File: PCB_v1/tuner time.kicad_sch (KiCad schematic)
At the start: 1 part, among them J2 1051640001

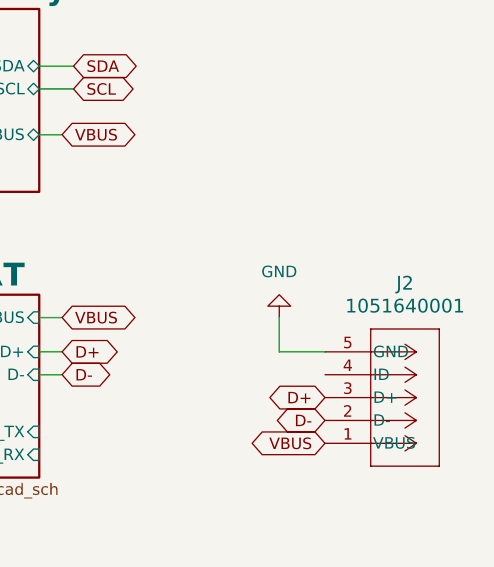
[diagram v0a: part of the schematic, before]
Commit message: adding the parts library
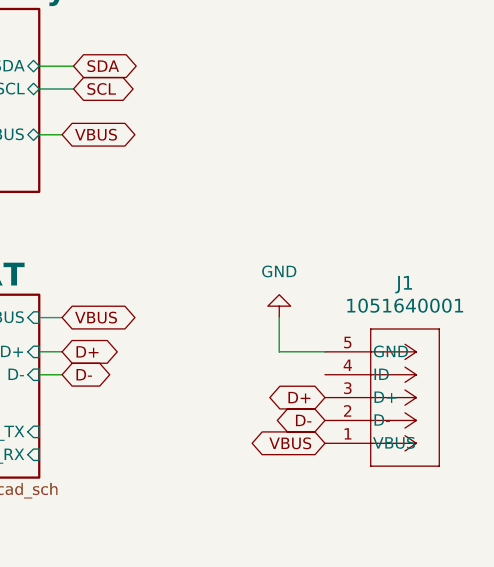
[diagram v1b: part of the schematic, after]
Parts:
- renumbered J2 to J1
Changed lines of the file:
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@@
 		(dnp no)
 		(fields_autoplaced yes)
-		(property "Reference" "#PWR093"
+		(property "Reference" "#PWR05"
 			(at 82.55 151.13 0)
 			(effects
@@
 			(project "tuner time"
 				(path "/353cef6a-fb6e-40d9-89f8-eb54b7aa5118"
-					(reference "#PWR093")
+					(reference "#PWR05")
 					(unit 1)
 				)
@@
 		(on_board yes)
 		(dnp no)
-		(property "Reference" "#PWR0105"
+		(property "Reference" "#PWR06"
 			(at 166.37 31.75 0)
 			(effects
@@
 			(project "tuner time"
 				(path "/353cef6a-fb6e-40d9-89f8-eb54b7aa5118"
-					(reference "#PWR0105")
+					(reference "#PWR06")
 					(unit 1)
 				)
@@
 		(on_board yes)
 		(dnp no)
-		(property "Reference" "#PWR094"
+		(property "Reference" "#PWR01"
 			(at 73.66 135.89 0)
 			(effects
@@
 			(project "tuner time"
 				(path "/353cef6a-fb6e-40d9-89f8-eb54b7aa5118"
-					(reference "#PWR094")
+					(reference "#PWR01")
 					(unit 1)
 				)
@@
 		(dnp no)
 		(fields_autoplaced yes)
-		(property "Reference" "#PWR0104"
+		(property "Reference" "#PWR08"
 			(at 171.45 45.72 0)
 			(effects
@@
 			(project "tuner time"
 				(path "/353cef6a-fb6e-40d9-89f8-eb54b7aa5118"
-					(reference "#PWR0104")
+					(reference "#PWR08")
 					(unit 1)
 				)
@@
 		(on_board yes)
 		(dnp no)
-		(property "Reference" "#PWR095"
+		(property "Reference" "#PWR04"
 			(at 80.01 132.08 0)
 			(effects
@@
 			(project "tuner time"
 				(path "/353cef6a-fb6e-40d9-89f8-eb54b7aa5118"
-					(reference "#PWR095")
+					(reference "#PWR04")
 					(unit 1)
 				)
@@
 		(on_board yes)
 		(dnp no)
-		(property "Reference" "#PWR0101"
+		(property "Reference" "#PWR09"
 			(at 171.45 57.15 0)
 			(effects
@@
 			(project "tuner time"
 				(path "/353cef6a-fb6e-40d9-89f8-eb54b7aa5118"
-					(reference "#PWR0101")
+					(reference "#PWR09")
 					(unit 1)
 				)
@@
 		(dnp no)
 		(fields_autoplaced yes)
-		(property "Reference" "#PWR098"
+		(property "Reference" "#PWR011"
 			(at 214.63 161.29 0)
 			(effects
@@
 			(project "tuner time"
 				(path "/353cef6a-fb6e-40d9-89f8-eb54b7aa5118"
-					(reference "#PWR098")
+					(reference "#PWR011")
 					(unit 1)
 				)
@@
 		(dnp no)
 		(fields_autoplaced yes)
-		(property "Reference" "J2"
+		(property "Reference" "J1"
 			(at 248.92 50.8 0)
 			(effects
@@
 			(project "tuner time"
 				(path "/353cef6a-fb6e-40d9-89f8-eb54b7aa5118"
-					(reference "J2")
+					(reference "J1")
 					(unit 1)
 				)
@@
 		(on_board yes)
 		(dnp no)
-		(property "Reference" "#PWR096"
+		(property "Reference" "#PWR012"
 			(at 214.63 146.05 0)
 			(effects
@@
 			(project "tuner time"
 				(path "/353cef6a-fb6e-40d9-89f8-eb54b7aa5118"
-					(reference "#PWR096")
+					(reference "#PWR012")
 					(unit 1)
 				)
@@
 		(on_board yes)
 		(dnp no)
-		(property "Reference" "#PWR097"
+		(property "Reference" "#PWR013"
 			(at 219.71 148.59 0)
 			(effects
@@
 			(project "tuner time"
 				(path "/353cef6a-fb6e-40d9-89f8-eb54b7aa5118"
-					(reference "#PWR097")
+					(reference "#PWR013")
 					(unit 1)
 				)
@@
 		(dnp no)
 		(fields_autoplaced yes)
-		(property "Reference" "#PWR0102"
+		(property "Reference" "#PWR010"
 			(at 171.45 78.74 0)
 			(effects
@@
 			(project "tuner time"
 				(path "/353cef6a-fb6e-40d9-89f8-eb54b7aa5118"
-					(reference "#PWR0102")
+					(reference "#PWR010")
 					(unit 1)
 				)
@@
 		(dnp no)
 		(fields_autoplaced yes)
-		(property "Reference" "#PWR0100"
+		(property "Reference" "#PWR03"
 			(at 80.01 82.55 0)
 			(effects
@@
 			(project "tuner time"
 				(path "/353cef6a-fb6e-40d9-89f8-eb54b7aa5118"
-					(reference "#PWR0100")
+					(reference "#PWR03")
 					(unit 1)
 				)
@@
 		(on_board yes)
 		(dnp no)
-		(property "Reference" "#PWR099"
+		(property "Reference" "#PWR02"
 			(at 80.01 64.77 0)
 			(effects
@@
 			(project "tuner time"
 				(path "/353cef6a-fb6e-40d9-89f8-eb54b7aa5118"
-					(reference "#PWR099")
+					(reference "#PWR02")
 					(unit 1)
 				)
@@
 		(dnp no)
 		(fields_autoplaced yes)
-		(property "Reference" "#PWR039"
+		(property "Reference" "#PWR014"
 			(at 234.95 48.26 0)
 			(effects
@@
 			(project "tuner time"
 				(path "/353cef6a-fb6e-40d9-89f8-eb54b7aa5118"
-					(reference "#PWR039")
+					(reference "#PWR014")
 					(unit 1)
 				)
@@
 		(on_board yes)
 		(dnp no)
-		(property "Reference" "#PWR0103"
+		(property "Reference" "#PWR07"
 			(at 171.45 27.94 0)
 			(effects
@@
 			(project "tuner time"
 				(path "/353cef6a-fb6e-40d9-89f8-eb54b7aa5118"
-					(reference "#PWR0103")
-					(unit 1)
-				)
+					(reference "#PWR07")
+					(unit 1)
+				)

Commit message: PCB updates
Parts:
- removed J1: 1051640001, CON00906_5_MOL, symbol 2025-02-12_14-59-21:1051640001
- added D1, D6: Green, LED_SMD:LED_0805_2012Metric_Pad1.15x1.40mm_HandSolder, symbol Device:LED
- added D7: Orange, LED_SMD:LED_0805_2012Metric_Pad1.15x1.40mm_HandSolder, symbol Device:LED
- added JP1: M1, Jumper:SolderJumper-3_P1.3mm_Open_RoundedPad1.0x1.5mm, symbol Jumper:SolderJumper_3_Open
- added JP2: M2, Jumper:SolderJumper-3_P1.3mm_Open_RoundedPad1.0x1.5mm, symbol Jumper:SolderJumper_3_Open
- added JP3: SLP, Jumper:SolderJumper-3_P1.3mm_Bridged12_RoundedPad1.0x1.5mm, symbol Jumper:SolderJumper_3_Bridged12
- added R1: 680, Resistor_SMD:R_0805_2012Metric, symbol Device:R_US
- added R31, R32: 680, Resistor_SMD:R_0805_2012Metric, symbol Device:R
- added TP1, TP2: ~, TestPoint:TestPoint_THTPad_D1.0mm_Drill0.5mm, symbol Connector:TestPoint
- added U1: C1F 2, C1_BEL, symbol GT_LIbrary:C1F_2
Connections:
- net 3V3: now also D6.2 (A)
- net 5V: now also D7.2 (A), JP1.1 (A), JP2.1 (A), JP3.1 (A), U1.1
- net GND: now also JP1.3 (B), JP2.3 (B), JP3.3 (B), R1.2, R31.1, R32.1
- net Motor/EN: now also TP2.1
- net Motor/FLT: now also D1.2 (A)
- net Motor/M0: now also JP2.2 (C)
- net Motor/M1: now also JP1.2 (C)
- net Motor/SLP: now also JP3.2 (C)
- net Motor/VMOT: now also U1.2
- net Motor/VREF: now also TP1.1
- new net: D7.1 (K), R31.2
- new net: D6.1 (K), R32.2
- new net: D1.1 (K), R1.1
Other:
- removed sheet USB to UART
- added sheet USB (USB.kicad_sch)
- sheet MCU ports: added DIR, I2S2_CLK, I2S2_SD, I2S2_WS, STEP, UART2_RX, UART2_TX; removed none
- sheet Motor ports: added AGND; removed CFG, GND
- sheet Power Delivery ports: added AGND; removed none

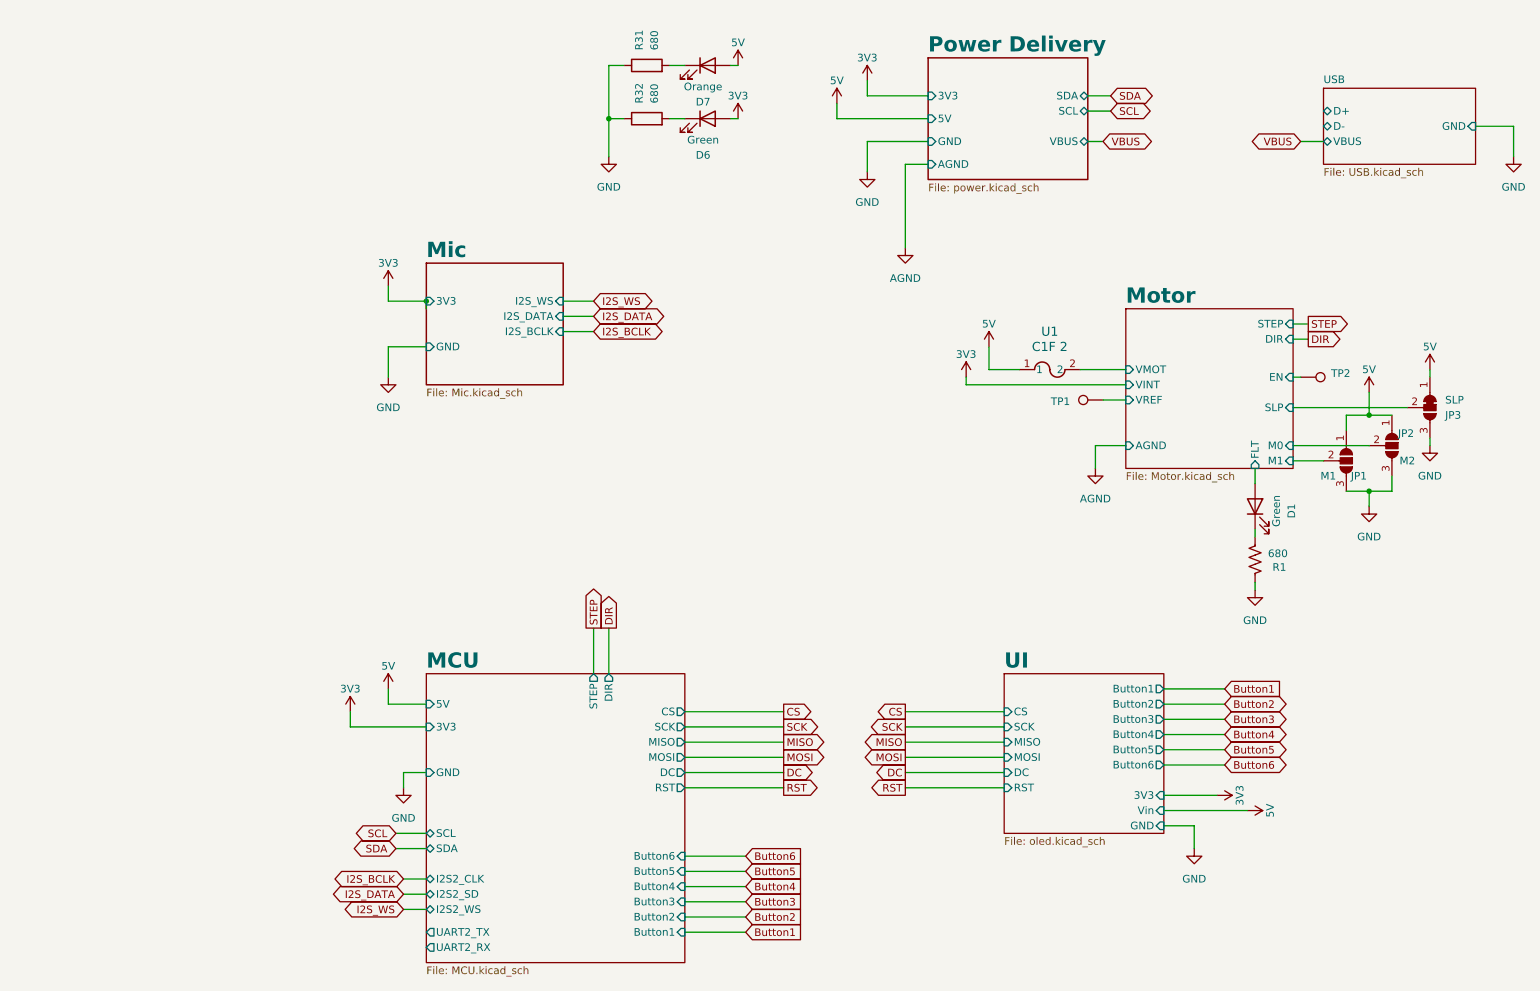
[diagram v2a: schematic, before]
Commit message: adjusted placments
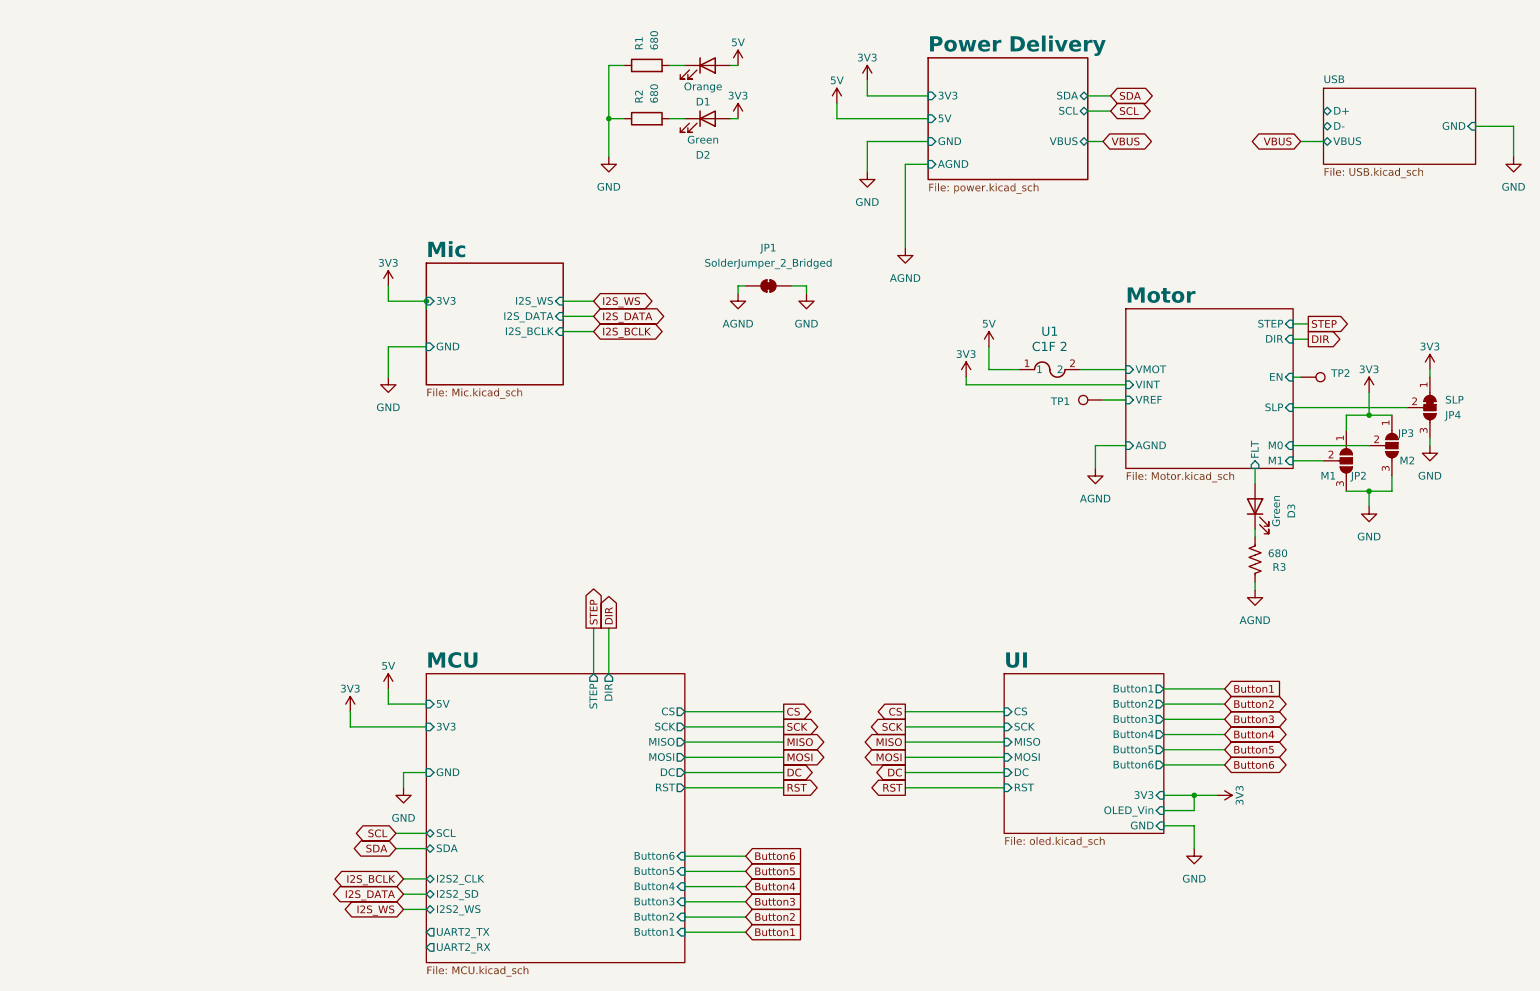
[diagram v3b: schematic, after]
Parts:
- added JP1: SolderJumper_2_Bridged, Jumper:SolderJumper-2_P1.3mm_Bridged2Bar_RoundedPad1.0x1.5mm, symbol Jumper:SolderJumper_2_Bridged
- renumbered D7 to D1, D6 to D2, D1 to D3, JP1 to JP2, JP2 to JP3, JP3 to JP4, R31 to R1, R32 to R2, R1 to R3
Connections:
- net 3V3: now also JP2.1 (A), JP3.1 (A), JP4.1 (A)
- net 5V: no longer JP2.1 (A), JP3.1 (A), JP4.1 (A)
- net AGND: now also R3.2, JP1.1 (A)
- net GND: now also JP1.2 (B); no longer R3.2
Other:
- sheet UI ports: added OLED_Vin; removed Vin
